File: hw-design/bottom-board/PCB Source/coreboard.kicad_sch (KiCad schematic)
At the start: 30 parts, among them J3 AS0A823-H4SB-7H, J5 HMI_DATA, J6 SERIAL_DEBUG, U7 AT24CS08

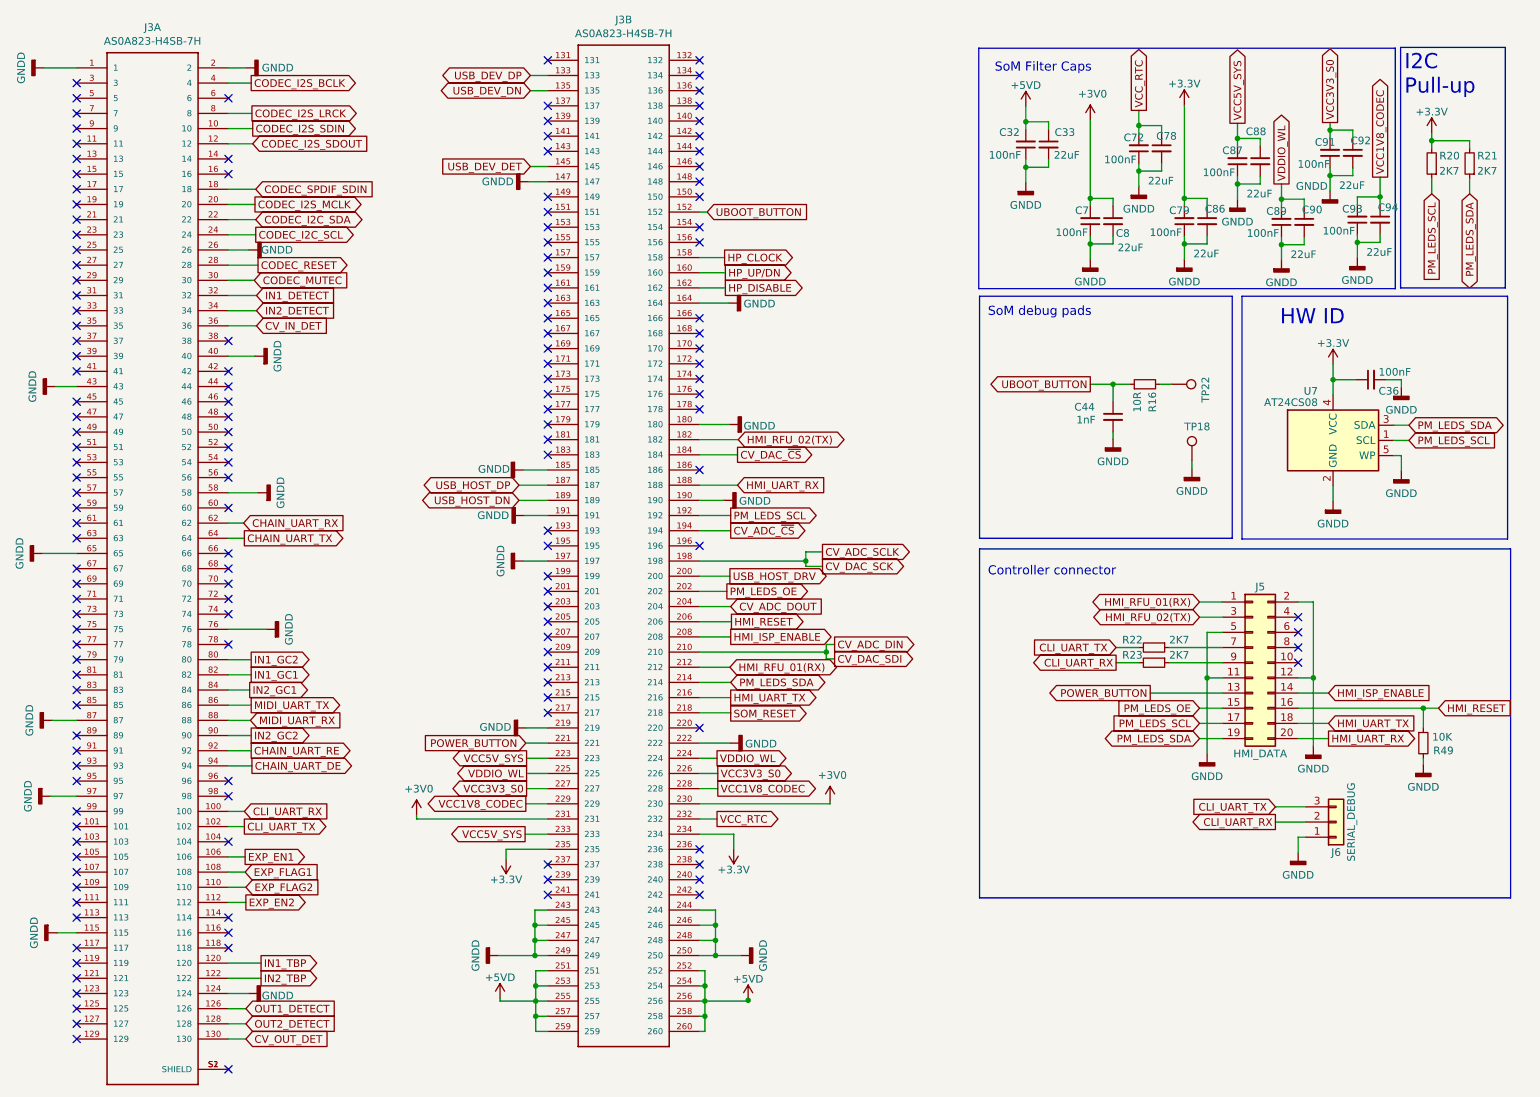
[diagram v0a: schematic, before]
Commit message: connect 5VD with 5V_SYS (otherwise ff-rk3399 doesnt boot)
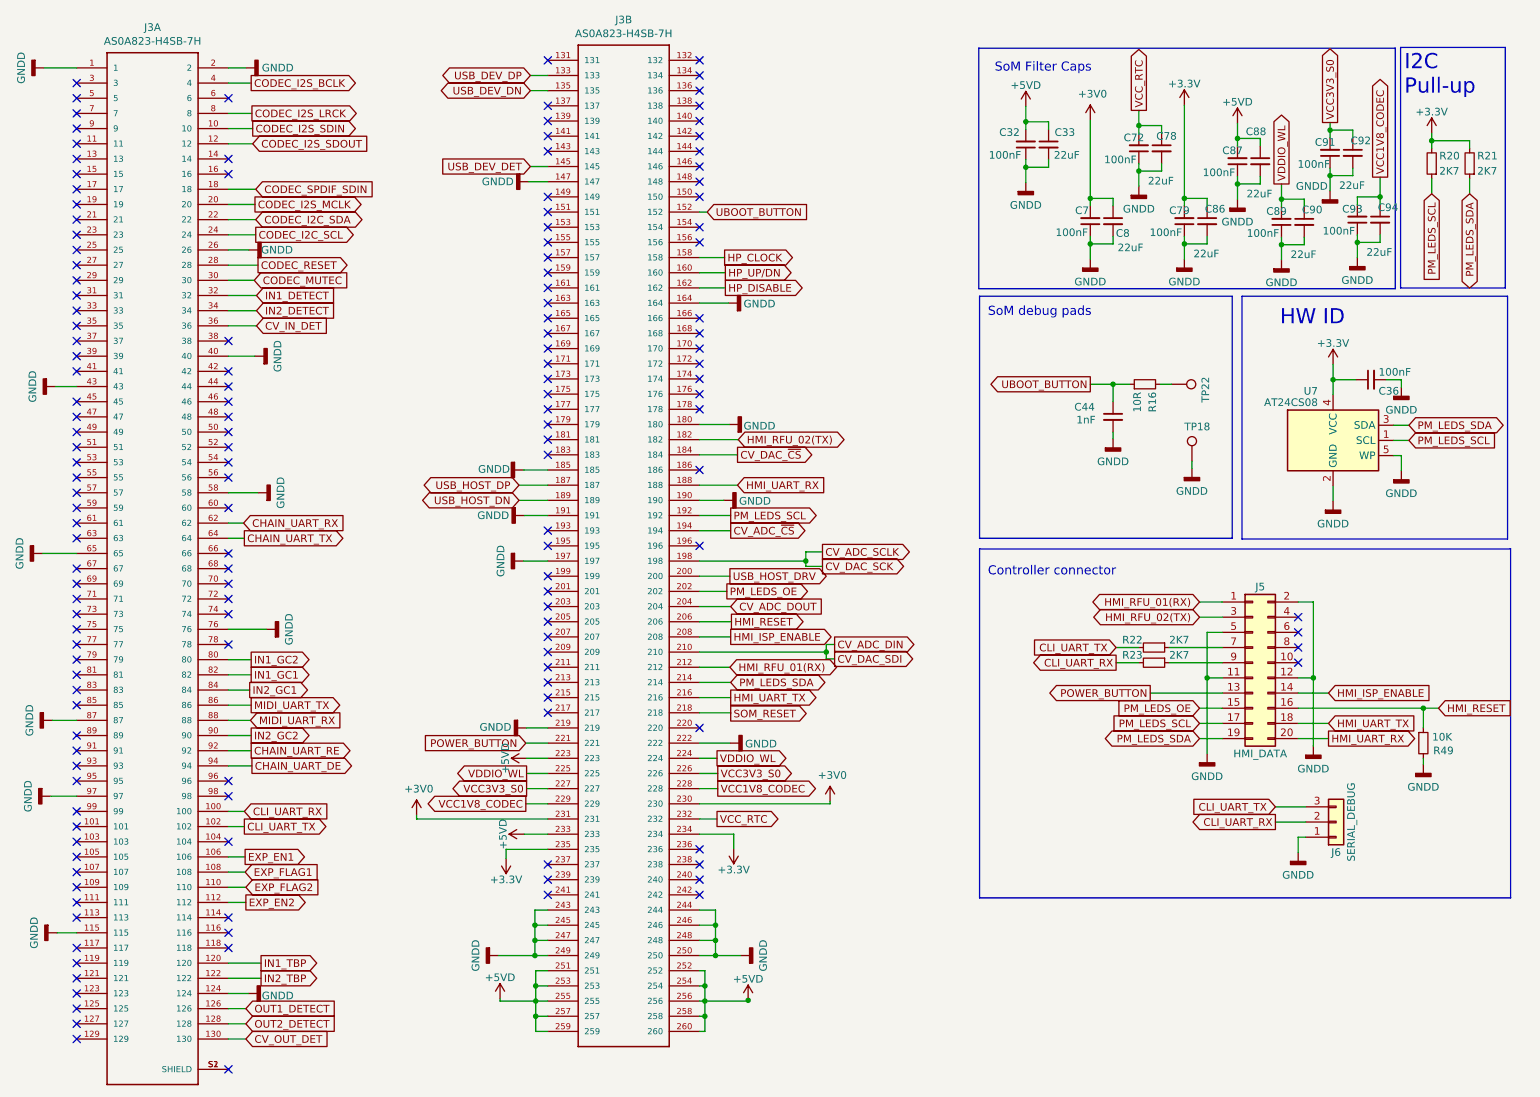
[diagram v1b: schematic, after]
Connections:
- net VCC5V_SYS is gone; now on net +5VD: C87.2, C88.1, J3.223, J3.233
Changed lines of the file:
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@@
+    (stroke (width 0) (type default) (color 0 0 0 0))
+  )
+  (wire (pts (xy 116.84 153.416) (xy 120.777 153.416))
     (stroke (width 0) (type default) (color 0 0 0 0))
   )
@@
   )
   (wire (pts (xy 146.177 153.416) (xy 151.892 153.416))
-    (stroke (width 0) (type default) (color 0 0 0 0))
-  )
-  (wire (pts (xy 120.777 153.416) (xy 116.967 153.416))
     (stroke (width 0) (type default) (color 0 0 0 0))
   )
@@
     )
   )
-  (global_label "VCC5V_SYS" (shape output) (at 117.221 140.716 180) (fields_autoplaced)
-    (effects (font (size 1.27 1.27)) (justify right))
-    (property "Intersheet References" "${INTERSHEET_REFS}" (id 0) (at 0 0 0)
-      (effects (font (size 1.27 1.27)) hide)
-    )
-  )
   (global_label "HP_DISABLE" (shape output) (at 150.495 61.976 0) (fields_autoplaced)
     (effects (font (size 1.27 1.27)) (justify left))
@@
   (global_label "CODEC_I2S_MCLK" (shape output) (at 71.755 48.006 0) (fields_autoplaced)
     (effects (font (size 1.27 1.27)) (justify left))
-    (property "Intersheet References" "${INTERSHEET_REFS}" (id 0) (at 0 0 0)
-      (effects (font (size 1.27 1.27)) hide)
-    )
-  )
-  (global_label "VCC5V_SYS" (shape output) (at 116.967 153.416 180) (fields_autoplaced)
-    (effects (font (size 1.27 1.27)) (justify right))
     (property "Intersheet References" "${INTERSHEET_REFS}" (id 0) (at 0 0 0)
       (effects (font (size 1.27 1.27)) hide)
@@
   )
   (global_label "CODEC_I2C_SCL" (shape output) (at 71.882 53.086 0) (fields_autoplaced)
-    (effects (font (size 1.27 1.27)) (justify left))
-    (property "Intersheet References" "${INTERSHEET_REFS}" (id 0) (at 0 0 0)
-      (effects (font (size 1.27 1.27)) hide)
-    )
-  )
-  (global_label "VCC5V_SYS" (shape output) (at 236.22 34.417 90) (fields_autoplaced)
     (effects (font (size 1.27 1.27)) (justify left))
     (property "Intersheet References" "${INTERSHEET_REFS}" (id 0) (at 0 0 0)
@@
       (effects (font (size 1.27 1.27)) hide)
     )
+    (pin "1")
+  )
+  (symbol (lib_id "bottom-board-rescue:+5VD-power") (at 117.221 140.716 90) (unit 1)
+    (in_bom yes) (on_board yes)
+    (property "Reference" "#PWR0319" (id 0) (at 121.031 140.716 0)
+      (effects (font (size 1.27 1.27)) hide)
+    )
+    (property "Value" "+5VD" (id 1) (at 113.665 140.716 0))
+    (property "Footprint" "" (id 2) (at 117.221 140.716 0)
+      (effects (font (size 1.27 1.27)) hide)
+    )
+    (property "Datasheet" "" (id 3) (at 117.221 140.716 0)
+      (effects (font (size 1.27 1.27)) hide)
+    )
+    (pin "1")
+  )
+  (symbol (lib_id "bottom-board-rescue:+5VD-power") (at 236.22 34.417 0) (unit 1)
+    (in_bom yes) (on_board yes)
+    (property "Reference" "#PWR0339" (id 0) (at 236.22 38.227 0)
+      (effects (font (size 1.27 1.27)) hide)
+    )
+    (property "Value" "+5VD" (id 1) (at 236.22 30.861 0))
+    (property "Footprint" "" (id 2) (at 236.22 34.417 0)
+      (effects (font (size 1.27 1.27)) hide)
+    )
+    (property "Datasheet" "" (id 3) (at 236.22 34.417 0)
+      (effects (font (size 1.27 1.27)) hide)
+    )
+    (pin "1")
+  )
+  (symbol (lib_id "bottom-board-rescue:+5VD-power") (at 116.84 153.416 90) (unit 1)
+    (in_bom yes) (on_board yes)
+    (property "Reference" "#PWR0338" (id 0) (at 120.65 153.416 0)
+      (effects (font (size 1.27 1.27)) hide)
+    )
+    (property "Value" "+5VD" (id 1) (at 113.284 153.416 0))
+    (property "Footprint" "" (id 2) (at 116.84 153.416 0)
+      (effects (font (size 1.27 1.27)) hide)
+    )
+    (property "Datasheet" "" (id 3) (at 116.84 153.416 0)
+      (effects (font (size 1.27 1.27)) hide)
+    )

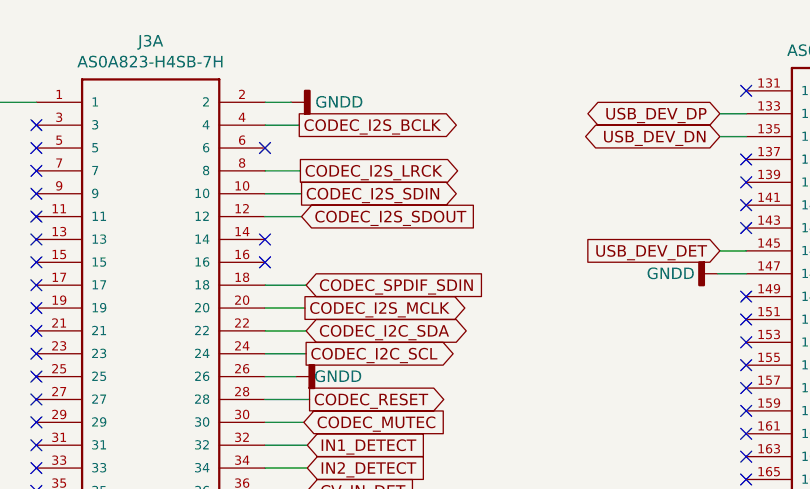
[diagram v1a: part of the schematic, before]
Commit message: correct i2s pins
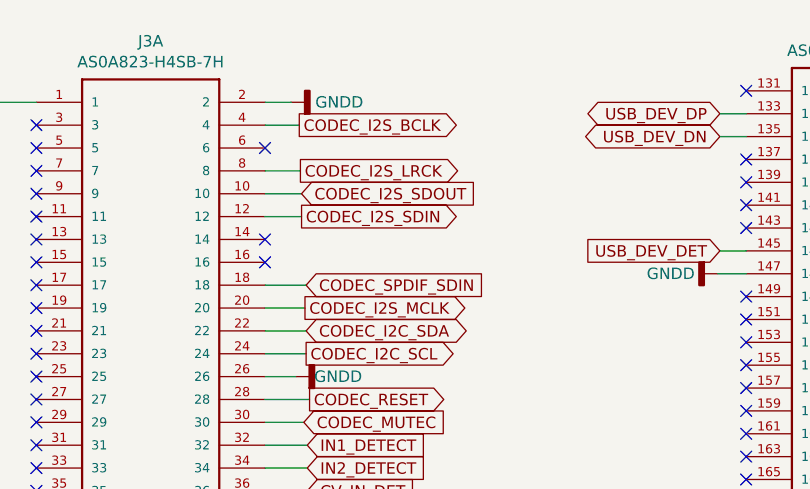
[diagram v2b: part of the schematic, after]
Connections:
- net CODEC_I2S_SDIN: now also J3.12; no longer J3.10
- net CODEC_I2S_SDOUT: now also J3.10; no longer J3.12
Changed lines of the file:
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@@
     )
   )
-  (global_label "CODEC_I2S_SDIN" (shape output) (at 71.374 35.306 0) (fields_autoplaced)
+  (global_label "CODEC_I2S_SDIN" (shape output) (at 71.374 37.846 0) (fields_autoplaced)
     (effects (font (size 1.27 1.27)) (justify left))
-    (property "Intersheet References" "${INTERSHEET_REFS}" (id 0) (at 0 0 0)
+    (property "Intersheet References" "${INTERSHEET_REFS}" (id 0) (at 0 2.54 0)
       (effects (font (size 1.27 1.27)) hide)
     )
@@
     )
   )
-  (global_label "CODEC_I2S_SDOUT" (shape input) (at 71.374 37.846 0) (fields_autoplaced)
+  (global_label "CODEC_I2S_SDOUT" (shape input) (at 71.374 35.306 0) (fields_autoplaced)
     (effects (font (size 1.27 1.27)) (justify left))
-    (property "Intersheet References" "${INTERSHEET_REFS}" (id 0) (at 0 0 0)
+    (property "Intersheet References" "${INTERSHEET_REFS}" (id 0) (at 0 -2.54 0)
       (effects (font (size 1.27 1.27)) hide)
     )

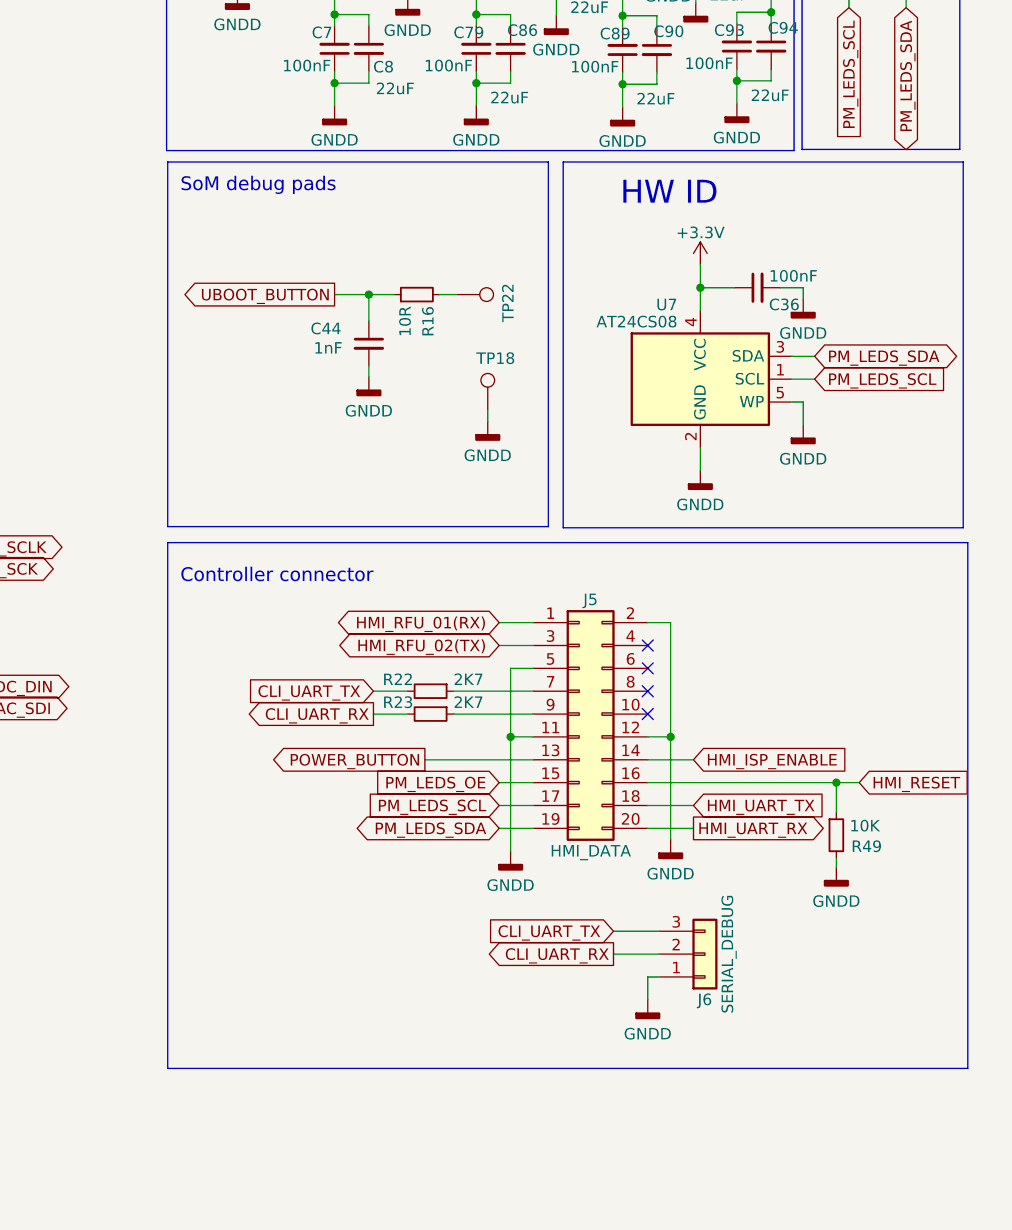
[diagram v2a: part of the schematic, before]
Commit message: change HMI connector type
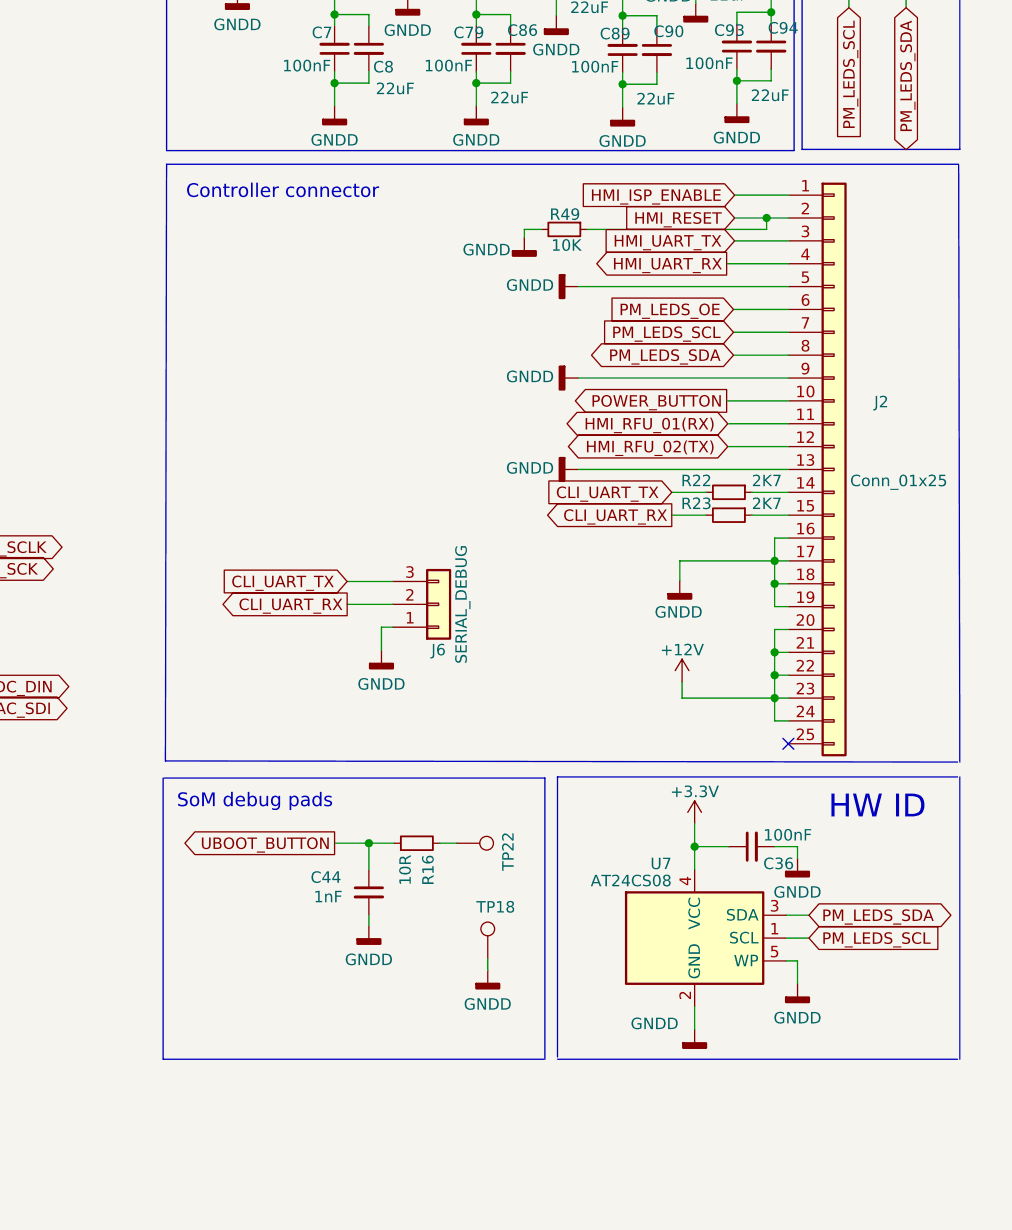
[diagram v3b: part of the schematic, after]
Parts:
- removed J5: HMI_DATA, footprints:Pin_Header_Straight_2x10_Shrouded, symbol bottom-board-rescue:Conn_02x10_Odd_Even-Connector_Generic
- added J2: Conn_01x25, F51L-1A7H1-11024:F51L-1A7H1-11024, symbol Connector_Generic:Conn_01x25
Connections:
- net GNDD: now also J2.13 (Pin_13), J2.16 (Pin_16), J2.17 (Pin_17), J2.18 (Pin_18), J2.19 (Pin_19), J2.5 (Pin_5), J2.9 (Pin_9)
- net HMI_ISP_ENABLE: now also J2.1 (Pin_1)
- net HMI_RESET: now also J2.2 (Pin_2)
- net HMI_RFU_01(RX): now also J2.11 (Pin_11)
- net HMI_RFU_02(TX): now also J2.12 (Pin_12)
- net HMI_UART_RX: now also J2.4 (Pin_4)
- net HMI_UART_TX: now also J2.3 (Pin_3)
- net PM_LEDS_OE: now also J2.6 (Pin_6)
- net PM_LEDS_SCL: now also J2.7 (Pin_7)
- net PM_LEDS_SDA: now also J2.8 (Pin_8)
- net POWER_BUTTON: now also J2.10 (Pin_10)
- net at R22.1: now also J2.14 (Pin_14)
- net at R23.1: now also J2.15 (Pin_15)
- new net +12V: J2.20 (Pin_20), J2.21 (Pin_21), J2.22 (Pin_22), J2.23 (Pin_23), J2.24 (Pin_24)
- no-connect marks 153 -> 150
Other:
- moved on the sheet: C36, C44, J6, R16, R22, R23, R49, TP18, TP22, U7

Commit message: fix issues reported by Kicad 6 RDC
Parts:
- J2: MPN (none) -> F51L-1A7H1-11024
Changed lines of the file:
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@@
       (effects (font (size 1.27 1.27)) hide)
+    )
+    (property "MPN" "F51L-1A7H1-11024" (id 4) (at 267.081 97.536 0)
+      (effects (font (size 1.524 1.524)) hide)
     )
     (pin "1")
